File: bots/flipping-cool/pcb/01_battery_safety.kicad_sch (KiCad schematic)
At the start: 8 parts, among them J1 XT30_BATTERY_IN_GNB4502S80AHV, J2 REMOVABLE_LINK_OR_RATED_SWITCH, J3 VISIBLE_POWER_LED_CURRENT_LIM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, J4 2S_BALANCE_SENSE_NO_CHARGE

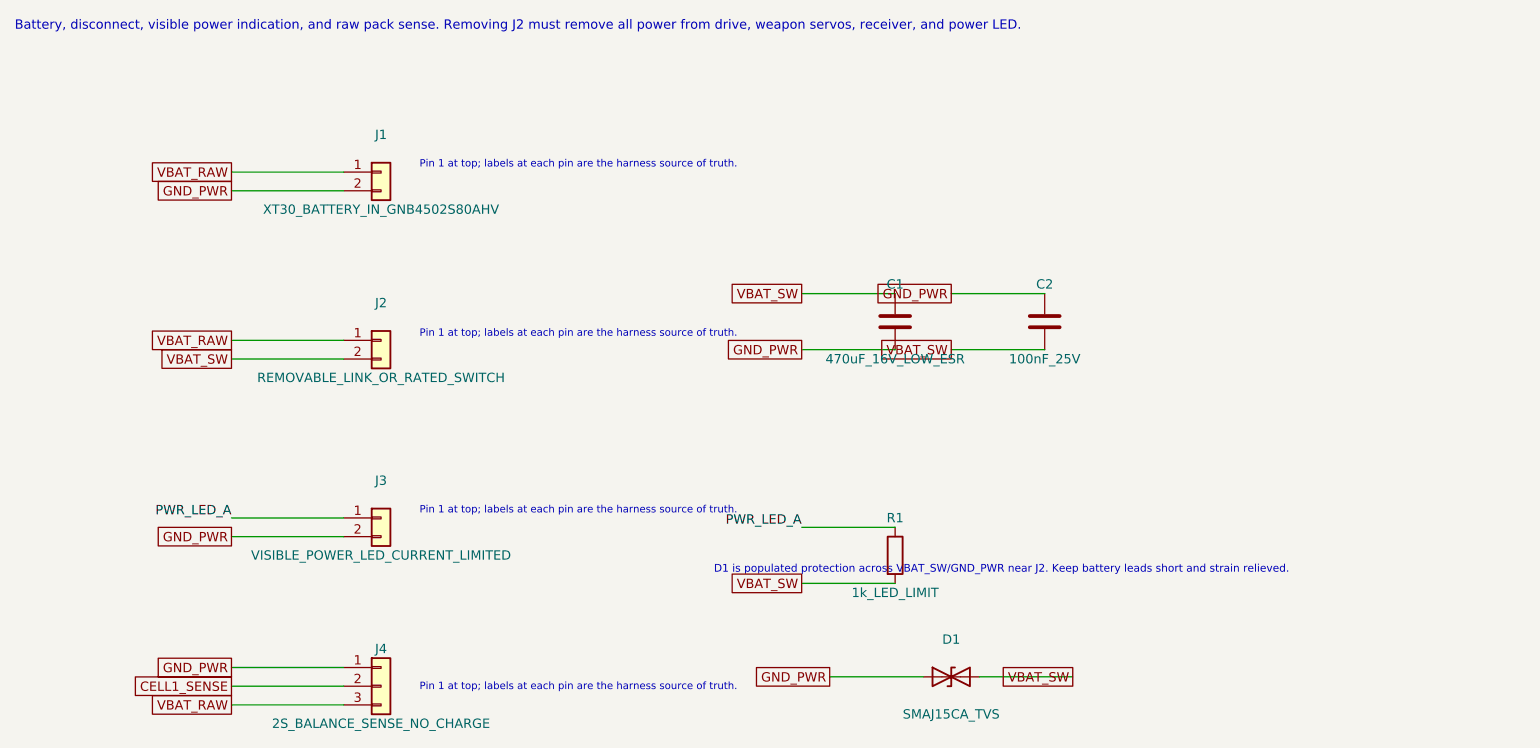
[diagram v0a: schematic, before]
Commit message: Refactor Flipping Cool PCB design to Rev B, updating title, date, and revision details. Integrate ESP32-S3 module and enhance documentation for MCU I/O and debugging features, while maintaining historical context from Rev A.
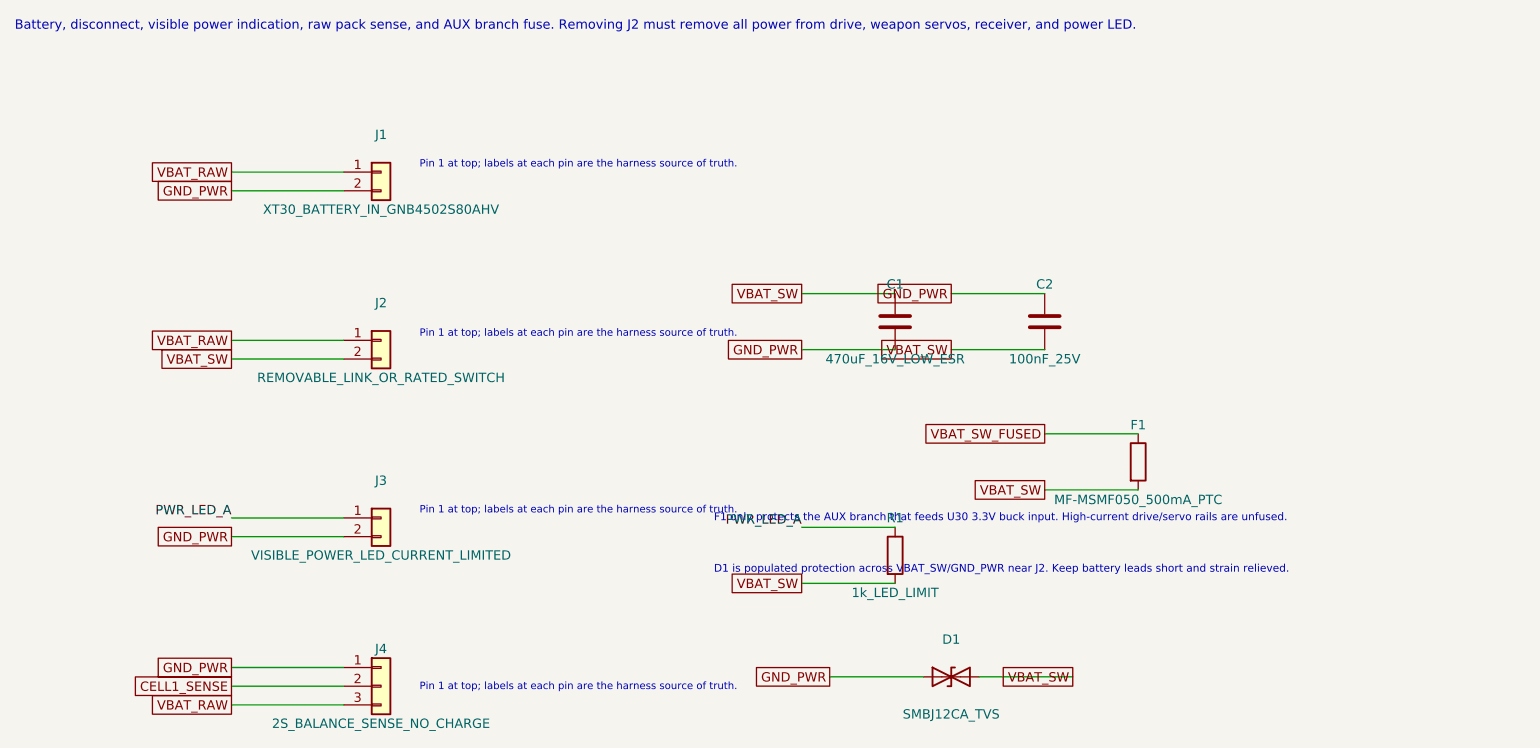
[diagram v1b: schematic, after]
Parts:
- added F1: MF-MSMF050_500mA_PTC, Fuse:Fuse_1812_4532Metric, symbol Device:R
- D1: value SMAJ15CA_TVS -> SMBJ12CA_TVS; footprint Diode_SMD:D_SMA -> Diode_SMD:D_SMB
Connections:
- net VBAT_SW: now also F1.2
- new net VBAT_SW_FUSED: F1.1
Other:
- note added: "Battery, disconnect, visible power indication, raw pack sense, and AUX branch fuse. Removing J2 must remove all power from drive, weapon servos, receiver, and power LED."
- note added: "F1 only protects the AUX branch that feeds U30 3.3V buck input. High-current drive/servo rails are unfused."
- note removed: "Battery, disconnect, visible power indication, and raw pack sense. Removing J2 must remove all power from drive, weapon servos, receiver, and power LED."

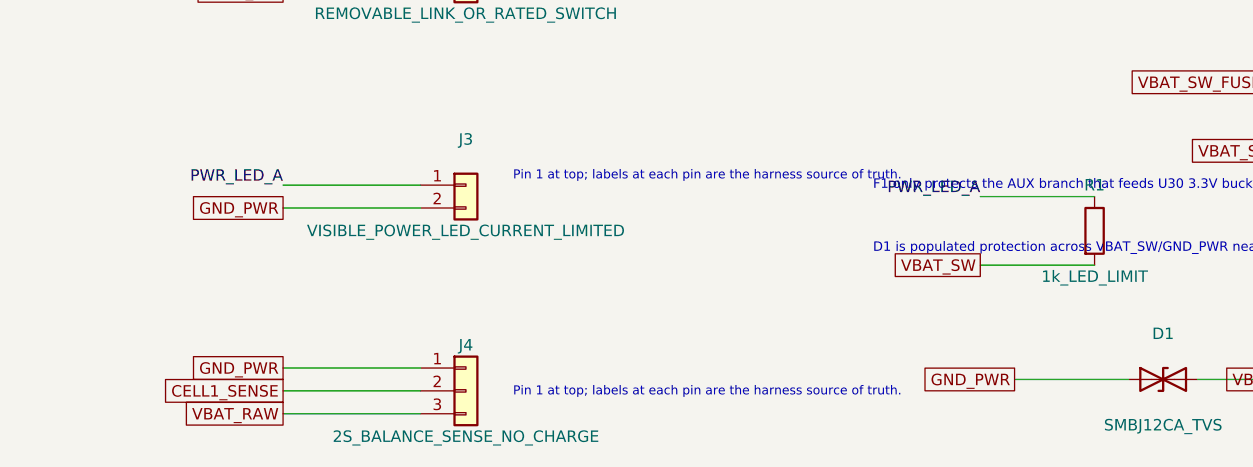
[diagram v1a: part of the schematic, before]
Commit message: Remove obsolete Flipping Cool Rev B project plan file and update schematic files to reflect the latest design changes, including integration of the ESP32-S3 module and enhancements to power management and control authority. Ensure all documentation is aligned with the current PCB design and architecture.
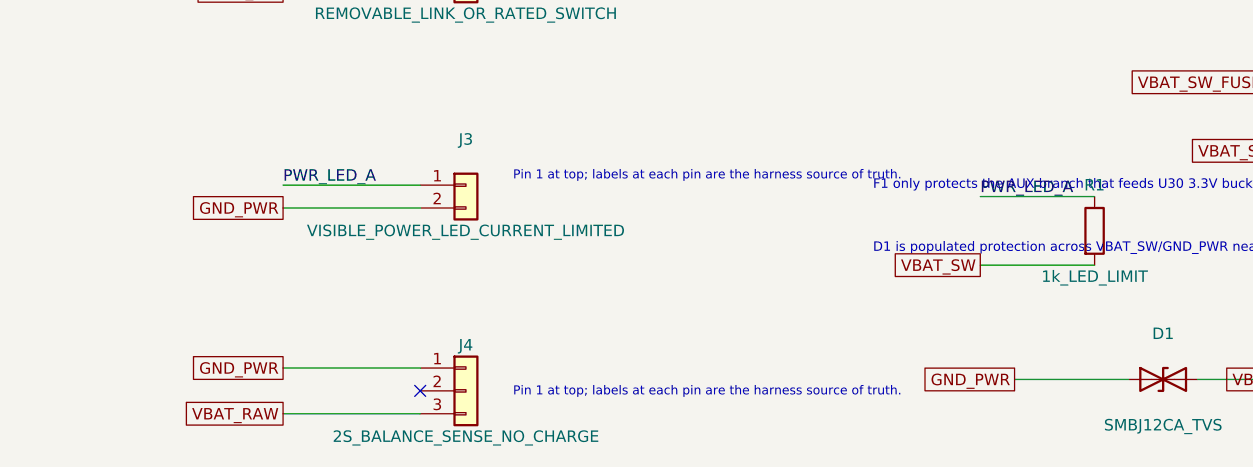
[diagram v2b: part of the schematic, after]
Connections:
- net CELL1_SENSE: no longer names the net of J4.2 (Pin_2)
- no-connect marks 0 -> 1
